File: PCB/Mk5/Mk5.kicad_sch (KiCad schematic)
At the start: 37 parts, among them J1 Power, J2 Bank, J25 HiAddr, J26 Expansion, J27 Conn_01x08_Pin, J3 Sync ~{NMI} ~{IRQ} RDY Gnd Ph2, J5 DISPLAY, SW1 RESET, U1 L7805, U2 DS1813, U25 GAL20V8B-10, U3 GAL20V8B-10, U4 R65C02, U5 EEPROM, U8 62256, Y25 1.8432 MHz

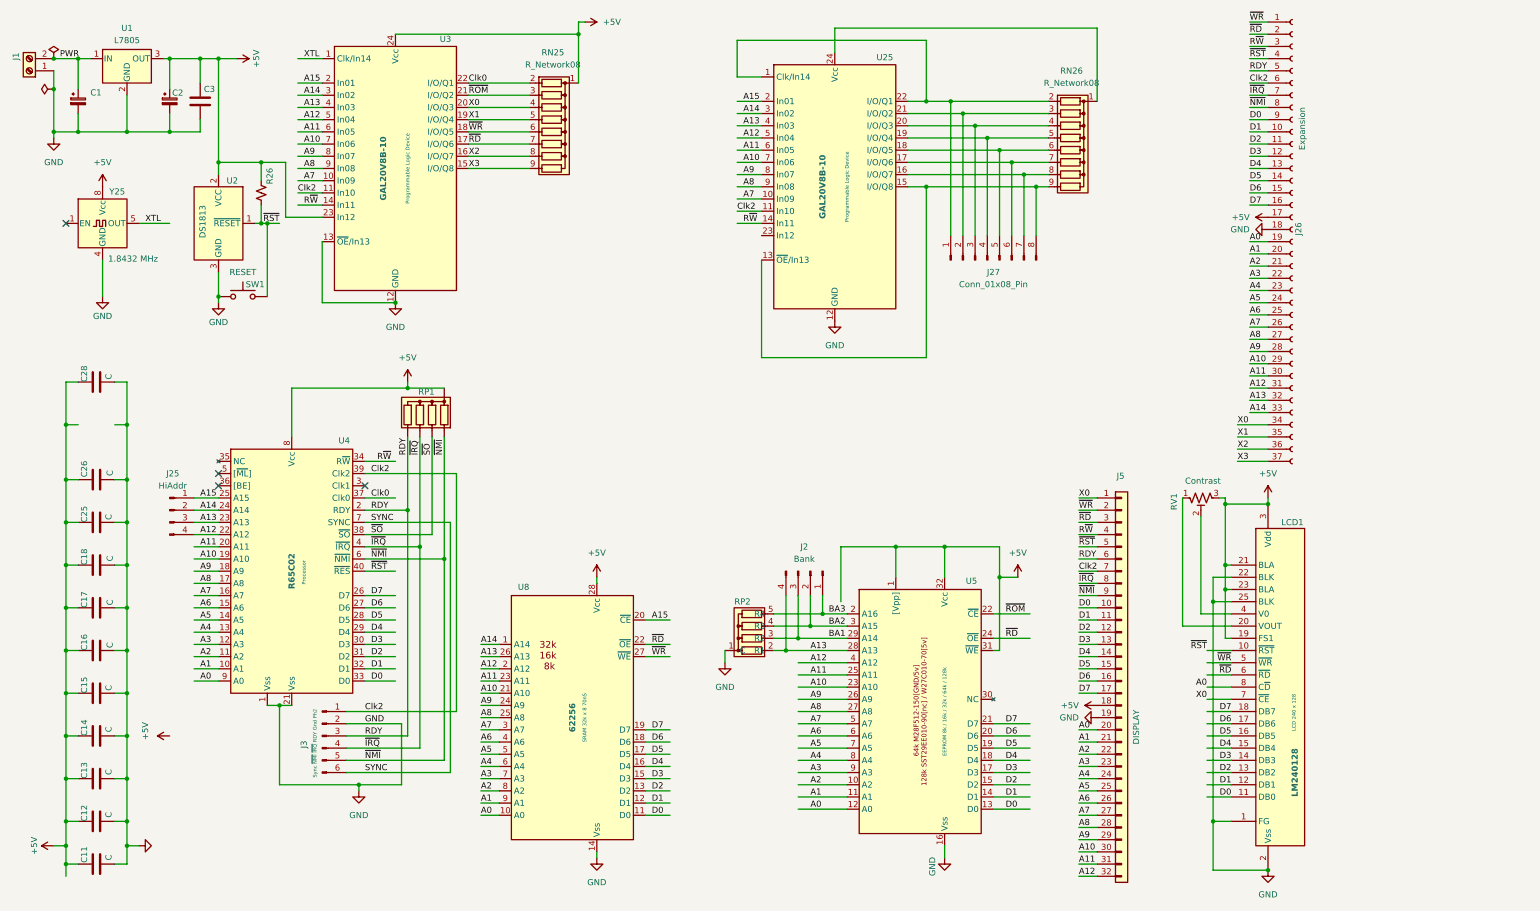
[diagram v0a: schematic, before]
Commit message: Added Mk4 (from retor) to add expansion bus as well
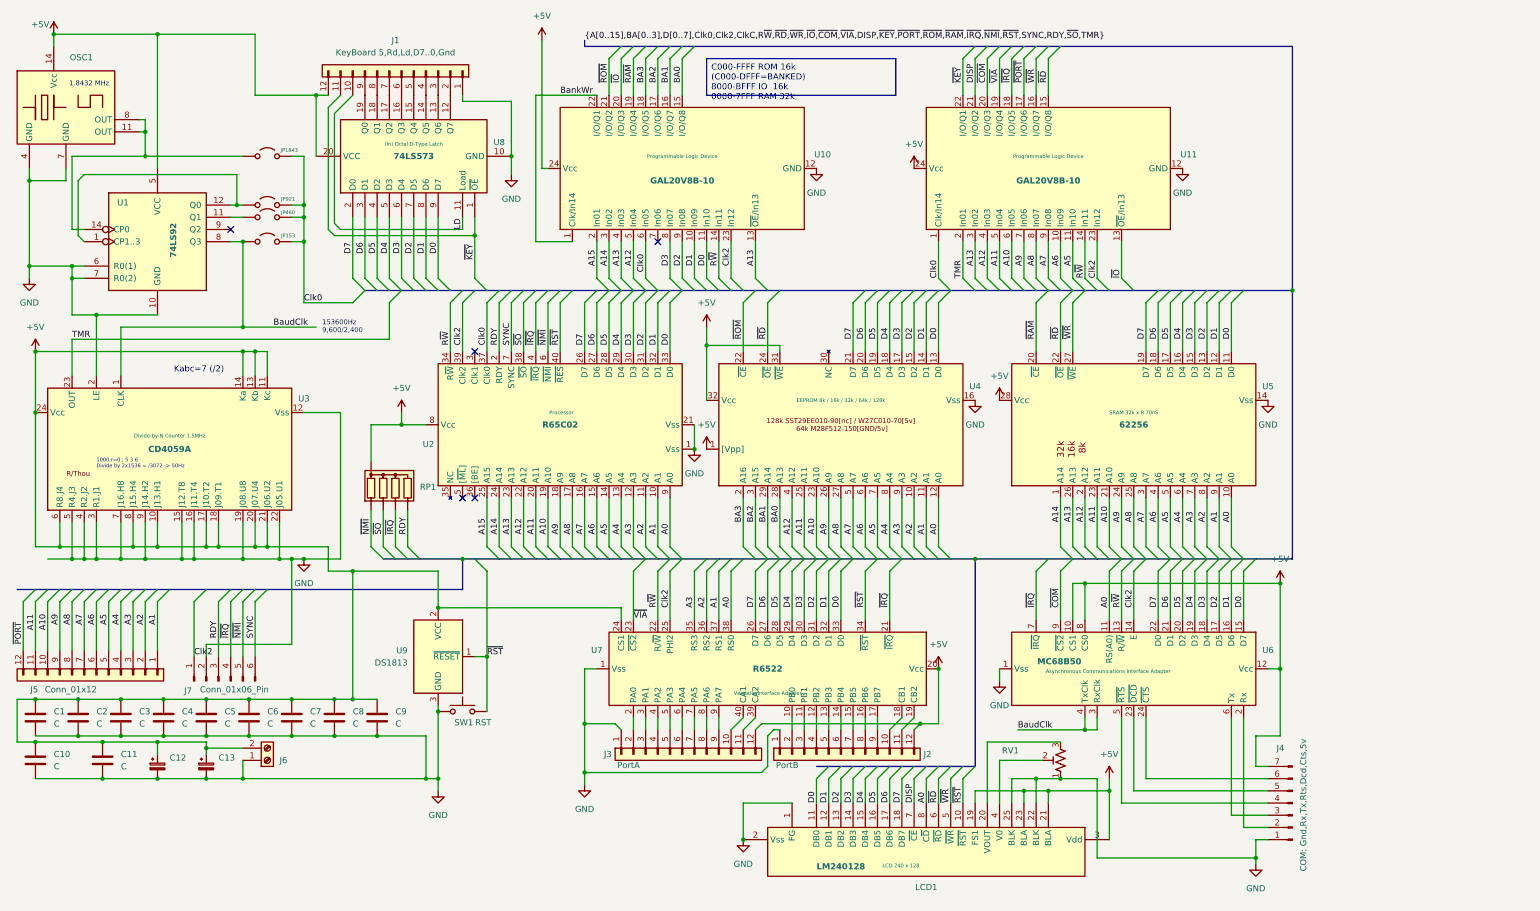
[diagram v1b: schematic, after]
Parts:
- removed C28: C, Capacitor_THT:C_Disc_D7.5mm_W2.5mm_P5.00mm, symbol Device:C
- removed J2: Bank, Connector_PinHeader_2.54mm:PinHeader_1x04_P2.54mm_Vertical, symbol Connector:Conn_01x04_Pin
- removed J25: HiAddr, symbol Connector:Conn_01x04_Pin
- removed J26: Expansion, symbol Connector:Conn_01x37_Socket
- removed J27: Conn_01x08_Pin, symbol Connector:Conn_01x08_Pin
- removed J5: DISPLAY, Connector_PinSocket_2.54mm:PinSocket_1x32_P2.54mm_Vertical, symbol Connector_Generic:Conn_01x32
- removed R26: R_Small_US, Resistor_THT:R_Axial_DIN0204_L3.6mm_D1.6mm_P7.62mm_Horizontal, symbol Device:R_Small_US
- removed RN25, RN26: R_Network08, Resistor_THT:R_Array_SIP9, symbol Device:R_Network08
- removed RP2: ~, Resistor_THT:R_Array_SIP5, symbol RetroParts_Library:Res4
- removed U1: L7805, Package_TO_SOT_THT:TO-220-3_Vertical, symbol Regulator_Linear:L7805
- removed U25: GAL20V8B-10, Package_DIP:DIP-24_W7.62mm_LongPads, symbol RetroParts_Library:GAL20v8
- removed Y25: 1.8432 MHz, Oscillator:Oscillator_DIP-8, symbol Oscillator:CXO_DIP8
- added J1: KeyBoard 5,Rd,Ld,D7..0,Gnd, Connector_PinHeader_2.54mm:PinHeader_1x12_P2.54mm_Vertical, symbol RetroParts_Library:Conn_01x12
- added J2: PortB, Connector_PinHeader_2.54mm:PinHeader_1x12_P2.54mm_Vertical, symbol RetroParts_Library:Conn_01x12
- added J3: PortA, Connector_PinHeader_2.54mm:PinHeader_1x12_P2.54mm_Vertical, symbol RetroParts_Library:Conn_01x12
- added J4: COM: Gnd,Rx,Tx,Rts,Dcd,Cts,5v, Connector_PinSocket_2.54mm:PinSocket_1x07_P2.54mm_Horizontal, symbol Connector:Conn_01x07_Pin
- added J5: Conn_01x12, Connector_PinSocket_2.54mm:PinSocket_1x12_P2.54mm_Vertical, symbol RetroParts_Library:Conn_01x12
- added JP153, JP1843, JP460, JP921: Jumper_2_Open, Connector_PinHeader_2.54mm:PinHeader_1x02_P2.54mm_Vertical, symbol RetroParts_Library:Jumper_2_Open
- added OSC1: ~, Package_DIP:DIP-14_W7.62mm_LongPads, symbol RetroParts_Library:XOSC
- added U1: 74LS92, Package_DIP:DIP-14_W7.62mm, symbol RetroParts_Library:74LS92
- added U11: GAL20V8B-10, Package_DIP:DIP-24_W7.62mm_LongPads, symbol RetroParts_Library:GAL20v8
- added U3: CD4059A, Package_DIP:DIP-24_W7.62mm_LongPads, symbol RetroParts_Library:4059
- added U6: MC68B50, Package_DIP:DIP-24_W15.24mm_LongPads, symbol RetroParts_Library:MC68B50
- added U7: R6522, Package_DIP:DIP-40_W15.24mm_LongPads, symbol RetroParts_Library:R6522
- added U8: 74LS573, Package_DIP:DIP-20_W7.62mm_LongPads, symbol RetroParts_Library:74LS573
- C11: renamed from C3; footprint Capacitor_THT:C_Disc_D7.5mm_W2.5mm_P5.00mm -> Capacitor_THT:C_Rect_L11.0mm_W2.8mm_P10.00mm_MKT
- C2: renamed from C12; footprint Capacitor_THT:C_Disc_D7.5mm_W2.5mm_P5.00mm -> Capacitor_THT:C_Rect_L11.0mm_W2.8mm_P10.00mm_MKT
- C5: renamed from C15; footprint Capacitor_THT:C_Disc_D7.5mm_W2.5mm_P5.00mm -> Capacitor_THT:C_Rect_L11.0mm_W2.8mm_P10.00mm_MKT
- J6: renamed from J1; value Power -> Screw_Terminal_01x02
- J7: renamed from J3; value Sync ~{NMI} ~{IRQ} RDY Gnd Ph2 -> Conn_01x06_Pin
- RV1: value Contrast -> R_Trim; footprint Potentiometer_THT:Potentiometer_Piher_PT-15-V15_Vertical -> Potentiometer_THT:Potentiometer_Runtron_RM-065_Vertical
- SW1: value RESET -> RST; footprint Button_Switch_THT:SW_PUSH_1P1T_6x3.5mm_H4.3_APEM_MJTP1243 -> Library:MiniSwitch
- U9: renamed from U2; footprint Package_TO_SOT_THT:TO-92L_Wide -> Package_TO_SOT_THT:TO-92L_Inline
- renumbered C11 to C1, C26 to C10, C1 to C12, C2 to C13, C13 to C3, C14 to C4, C16 to C6, C17 to C7, C18 to C8, C25 to C9, U3 to U10, U4 to U2, U5 to U4, U8 to U5
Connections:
- net PWR is gone; now on net +5V: C12.1, J6.2 (Pin_2)
- net X2 is gone; now on net BA1: U10.16 (I/O/Q7)
- net +5V: now also J1.12 (Pin_12), J2.12 (Pin_12), J3.12 (Pin_12), J4.7 (Pin_7), OSC1.14 (Vcc), U1.5 (VCC), U11.24 (Vcc), U3.10 (J13.H1), U3.11 (Kc), U3.13 (Kb), U3.14 (Ka), U3.17 (J10.T2), U3.18 (J09.T1), U3.20 (J07.U4), U3.21 (J06.U2), U3.24 (Vcc), U3.6 (R8.J4), U3.8 (J15.H4), U6.10 (CS1), U6.12 (Vcc), U6.8 (CS0), U7.20 (Vcc), U7.24 (CS1), U8.20 (VCC); no longer RV1.3, U10.23 (In12)
- net A0: now also U6.11 (RS(A0)), U7.38 (RS0)
- net A1: now also J5.1 (Pin_1), U7.37 (RS1)
- net A10: now also J5.10 (Pin_10), U11.6 (In05); no longer U10.7 (In06)
- net A11: now also J5.11 (Pin_11), U11.5 (In04); no longer U10.6 (In05)
- net A12: now also U11.4 (In03)
- net A13: now also U10.13 (~{OE}/In13), U11.3 (In02); no longer U4.28 (A13)
- net A15: no longer U5.20 (~{CE})
- net A2: now also J5.2 (Pin_2), U7.36 (RS2)
- net A3: now also J5.3 (Pin_3), U7.35 (RS3)
- net A4: now also J5.4 (Pin_4)
- net A5: now also J5.5 (Pin_5), U11.11 (In10)
- net A6: now also J5.6 (Pin_6), U11.10 (In09)
- net A7: now also J5.7 (Pin_7), U11.9 (In08); no longer U10.10 (In09)
- net A9: now also J5.9 (Pin_9), U11.7 (In06); no longer U10.8 (In07)
- net BA2: now also U10.17 (I/O/Q6)
- net BA3: now also U10.18 (I/O/Q5)
- net Clk0: now also U10.6 (In05), JP153.2 (B), JP1843.2 (B), JP460.2 (B), JP921.2 (B), U11.1 (Clk/In14); no longer U10.22 (I/O/Q1)
- net Clk2: now also U10.23 (In12), U11.23 (In12), U6.14 (E), U7.25 (PHI2); no longer U10.11 (In10)
- net D0: now also U10.11 (In10), U6.15 (D7), U7.33 (D0), U8.9 (D7)
- net D1: now also U10.10 (In09), U6.16 (D6), U7.32 (D1), U8.8 (D6)
- net D2: now also U10.9 (In08), U6.17 (D5), U7.31 (D2), U8.7 (D5)
- net D3: now also U10.8 (In07), U6.18 (D4), U7.30 (D3), U8.6 (D4)
- net D4: now also U6.19 (D3), U7.29 (D4), U8.5 (D3)
- net D5: now also U6.20 (D2), U7.28 (D5), U8.4 (D2)
- net D6: now also U6.21 (D1), U7.27 (D6), U8.3 (D1)
- net D7: now also U6.22 (D0), U7.26 (D7), U8.2 (D0)
- net GND: now also RV1.1, J1.1 (Pin_1), J2.1 (Pin_1), J3.1 (Pin_1), J4.1 (Pin_1), OSC1.4 (GND), OSC1.7 (GND), U1.10 (GND), U1.6 (R0(1)), U1.7 (R0(2)), U11.12 (GND), U3.12 (Vss), U3.15 (J12.T8), U3.16 (J11.T4), U3.19 (J08.U8), U3.2 (LE), U3.22 (J05.U1), U3.3 (R1.J1), U3.4 (R2.J2), U3.5 (R4.J3), U3.7 (J16.H8), U3.9 (J14.H2), U6.1 (Vss), U7.1 (Vss), U8.10 (GND); no longer U10.13 (~{OE}/In13)
- net R~{W}: now also U11.14 (In11), U6.13 (R/~{W}), U7.22 (R/~{W})
- net ~{IRQ}: now also U11.18 (I/O/Q5), U6.7 (~{IRQ}), U7.21 (~{IRQ})
- net ~{RD}: now also U11.15 (I/O/Q8); no longer U10.17 (I/O/Q6)
- net ~{RST}: now also U7.34 (~{RST})
- net ~{WR}: now also U11.16 (I/O/Q7); no longer U10.18 (I/O/Q5)
- net at LCD1.20 (VOUT): now also RV1.3; no longer RV1.1
- net A8: now reaches U2.17 (A8), U4.27 (A8), U5.25 (A8)
- net A8: now also J5.8 (Pin_8), U11.8 (In07); no longer U10.9 (In08)
- net X0 renamed DISP
- net DISP: now also U11.21 (I/O/Q2); no longer U10.20 (I/O/Q3)
- net X1 renamed ~{RAM}
- net ~{RAM}: now also U5.20 (~{CE})
- net X3 renamed BA0
- net BA0: now also U4.28 (A13)
- net XTL renamed BankWr
- net BankWr: now also U10.22 (I/O/Q1)
- new net: J1.2 (Pin_2), U8.12 (Q7)
- new net: J1.3 (Pin_3), U8.13 (Q6)
- new net: J1.4 (Pin_4), U8.14 (Q5)
- new net: J1.5 (Pin_5), U8.15 (Q4)
- new net: J1.6 (Pin_6), U8.16 (Q3)
- new net: J1.7 (Pin_7), U8.17 (Q2)
- new net: J1.8 (Pin_8), U8.18 (Q1)
- new net: J1.9 (Pin_9), U8.19 (Q0)
- new net: J4.2 (Pin_2), U6.2 (Rx)
- new net: J4.3 (Pin_3), U6.6 (Tx)
- new net: J4.4 (Pin_4), U6.5 (~{RTS})
- new net: J4.5 (Pin_5), U6.23 (~{DCD})
- new net: J4.6 (Pin_6), U6.24 (~{CTS})
- new net: J2.2 (Pin_2), U7.10 (PB0)
- new net: J2.3 (Pin_3), U7.11 (PB1)
- new net: J2.4 (Pin_4), U7.12 (PB2)
- new net: J2.5 (Pin_5), U7.13 (PB3)
- new net: J2.6 (Pin_6), U7.14 (PB4)
- new net: J2.7 (Pin_7), U7.15 (PB5)
- new net: J2.8 (Pin_8), U7.16 (PB6)
- new net: J2.9 (Pin_9), U7.17 (PB7)
- new net: J2.10 (Pin_10), U7.18 (CB1)
- new net: J2.11 (Pin_11), U7.19 (CB2)
- new net: J3.2 (Pin_2), U7.2 (PA0)
- new net: J3.3 (Pin_3), U7.3 (PA1)
- new net: J3.11 (Pin_11), U7.39 (CA2)
- new net: J3.4 (Pin_4), U7.4 (PA2)
- new net: J3.10 (Pin_10), U7.40 (CA1)
- new net: J3.5 (Pin_5), U7.5 (PA3)
- new net: J3.6 (Pin_6), U7.6 (PA4)
- new net: J3.7 (Pin_7), U7.7 (PA5)
- new net: J3.8 (Pin_8), U7.8 (PA6)
- new net: J3.9 (Pin_9), U7.9 (PA7)
- new net: JP1843.1 (A), OSC1.11 (OUT), OSC1.8 (OUT), U1.14 (CP0)
- new net: JP460.1 (A), U1.11 (Q1)
- new net: JP921.1 (A), U1.1 (CP1..3), U1.12 (Q0)
- new net BaudClk: JP153.1 (A), U1.8 (Q3), U3.1 (CLK), U6.3 (RxClk), U6.4 (TxClk)
- new net LD: J1.10 (Pin_10), U8.11 (Load)
- new net TMR: U11.2 (In01), U3.23 (OUT)
- new net ~{COM}: U11.20 (I/O/Q3), U6.9 (~{CS2})
- new net ~{IO}: U10.20 (I/O/Q3), U11.13 (~{OE}/In13)
- new net ~{KEY}: J1.11 (Pin_11), U11.22 (I/O/Q1), U8.1 (~{OE})
- new net ~{PORT}: J5.12 (Pin_12), U11.17 (I/O/Q6)
- new net ~{VIA}: U11.19 (I/O/Q4), U7.23 (~{CS2})
- no-connect marks 4 -> 5
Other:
- note added: "1.8432 MHz"
- note added: "1000,r=0 ; 5 3 6 Divide by 2x1536 = /3072 -> 50Hz"
- note added: "153600Hz 9,600/2,400"
- note added: "Kabc=7 (/2)"
- moved on the sheet: C1, C10, C11, C12, C13, C2, C3, C4, C5, C6, C7, C8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
